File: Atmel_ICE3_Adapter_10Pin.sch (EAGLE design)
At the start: 2 parts

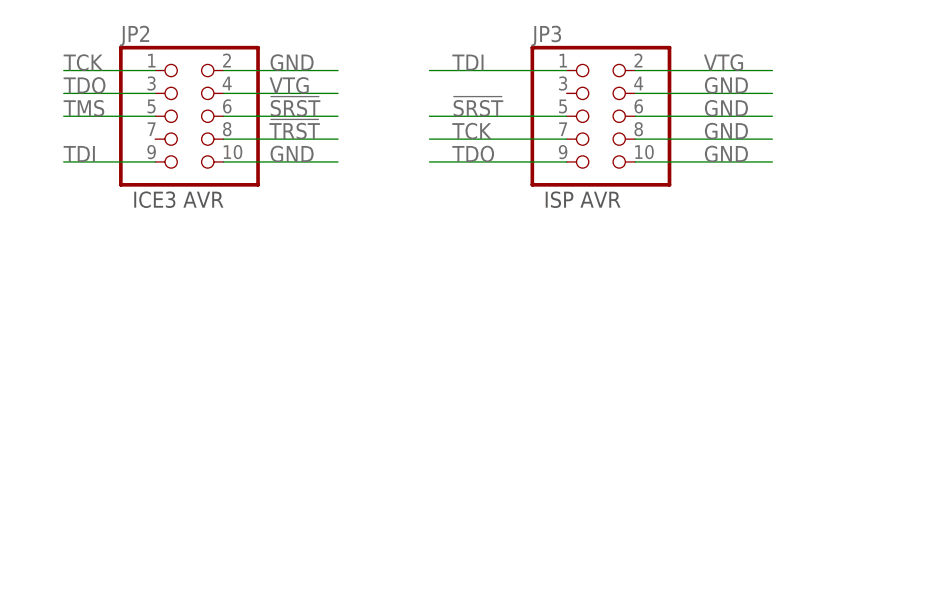
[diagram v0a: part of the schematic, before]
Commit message: Fix 6 pin wrong ICE3 header
Add 10 pin
Add gerber files
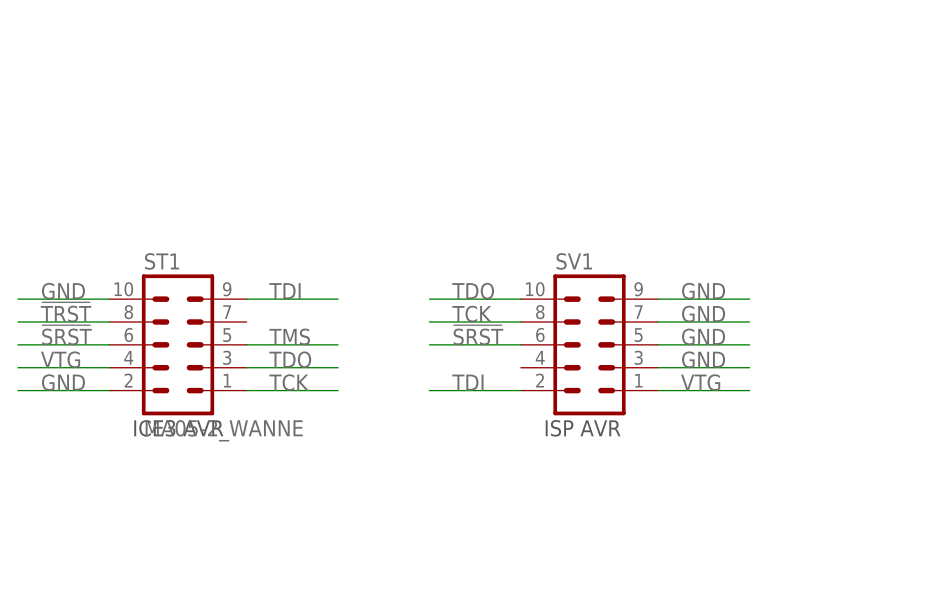
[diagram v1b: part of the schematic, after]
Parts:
- removed JP2: (no value), pinhead_2:PINHD-2X5_2.00
- removed JP3: (no value), pinhead_2:PINHD-2X5_2.54
- added ST1: MA05-2_WANNE, pin-header-1.27:MA05-2_WANNE
- added SV1: (no value), con-lstb:MA05-2
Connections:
- net !SRST: now also ST1.6, SV1.6; no longer JP2.6, JP3.5
- net !TRST: now also ST1.8; no longer JP2.8
- net GND: now also ST1.10, ST1.2, SV1.3, SV1.5, SV1.7, SV1.9; no longer JP2.10, JP2.2, JP3.10, JP3.4, JP3.6, JP3.8
- net TCK: now also ST1.1, SV1.8; no longer JP2.1, JP3.7
- net TDI: now also ST1.9, SV1.2; no longer JP2.9, JP3.1
- net TDO: now also ST1.3, SV1.10; no longer JP2.3, JP3.9
- net TMS: now also ST1.5; no longer JP2.5
- net VTG: now also ST1.4, SV1.1; no longer JP2.4, JP3.2
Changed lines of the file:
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@@
 </variantdefs>
 <classes>
-<class number="0" name="default" width="0.3" drill="0.3">
-<clearance class="0" value="0.3"/>
+<class number="0" name="default" width="0" drill="0">
 </class>
-<class number="1" name="pwr" width="0.5" drill="0.5">
-<clearance class="1" value="0.3"/>
+<class number="1" name="pwr" width="0" drill="0">
 </class>
 </classes>
 <parts>
-<part name="JP2" library="pinhead_2" deviceset="PINHD-2X5" device="_2.00"/>
-<part name="JP3" library="pinhead_2" deviceset="PINHD-2X5" device="_2.54"/>
 <part name="FRAME1" library="frames" deviceset="DINA4_L" device=""/>
+<part name="SV1" library="con-lstb" deviceset="MA05-2" device=""/>
+<part name="ST1" library="pin-header-1.27" deviceset="MA05-2_WANNE" device=""/>
 </parts>
 <sheets>
 <sheet>
 <plain>
-<text x="99.06" y="91.44" size="1.778" layer="97">ICE3 AVR</text>
-<text x="144.78" y="91.44" size="1.778" layer="97">ISP AVR</text>
+<text x="99.06" y="66.04" size="1.778" layer="97">ICE3 AVR</text>
+<text x="144.78" y="66.04" size="1.778" layer="97">ISP AVR</text>
 <text x="180.086" y="26.162" size="5.08" layer="97">Adapter ICE3 AVR</text>
 </plain>
 <instances>
-<instance part="JP2" gate="A" x="104.14" y="101.6"/>
-<instance part="JP3" gate="A" x="149.86" y="101.6"/>
 <instance part="FRAME1" gate="G$1" x="0" y="0"/>
 <instance part="FRAME1" gate="G$2" x="162.56" y="0"/>
+<instance part="SV1" gate="G$1" x="149.86" y="76.2"/>
+<instance part="ST1" gate="G$1" x="104.14" y="76.2"/>
 </instances>
 <busses>
@@
 <net name="TCK" class="0">
 <segment>
-<wire x1="101.6" y1="106.68" x2="91.44" y2="106.68" width="0.1524" layer="91"/>
-<label x="91.44" y="106.68" size="1.778" layer="95"/>
-<pinref part="JP2" gate="A" pin="1"/>
+<pinref part="SV1" gate="G$1" pin="8"/>
+<wire x1="142.24" y1="78.74" x2="132.08" y2="78.74" width="0.1524" layer="91"/>
+<label x="134.62" y="78.74" size="1.778" layer="95"/>
 </segment>
 <segment>
-<pinref part="JP3" gate="A" pin="7"/>
-<wire x1="147.32" y1="99.06" x2="132.08" y2="99.06" width="0.1524" layer="91"/>
-<label x="134.62" y="99.06" size="1.778" layer="95"/>
+<wire x1="111.76" y1="71.12" x2="121.92" y2="71.12" width="0.1524" layer="91"/>
+<label x="114.3" y="71.12" size="1.778" layer="95"/>
+<pinref part="ST1" gate="G$1" pin="1"/>
 </segment>
 </net>
 <net name="TDO" class="0">
 <segment>
-<wire x1="101.6" y1="104.14" x2="91.44" y2="104.14" width="0.1524" layer="91"/>
-<label x="91.44" y="104.14" size="1.778" layer="95"/>
-<pinref part="JP2" gate="A" pin="3"/>
+<pinref part="SV1" gate="G$1" pin="10"/>
+<wire x1="142.24" y1="81.28" x2="132.08" y2="81.28" width="0.1524" layer="91"/>
+<label x="134.62" y="81.28" size="1.778" layer="95"/>
 </segment>
 <segment>
-<pinref part="JP3" gate="A" pin="9"/>
-<wire x1="147.32" y1="96.52" x2="132.08" y2="96.52" width="0.1524" layer="91"/>
-<label x="134.62" y="96.52" size="1.778" layer="95"/>
+<wire x1="111.76" y1="73.66" x2="121.92" y2="73.66" width="0.1524" layer="91"/>
+<label x="114.3" y="73.66" size="1.778" layer="95"/>
+<pinref part="ST1" gate="G$1" pin="3"/>
 </segment>
 </net>
 <net name="TMS" class="0">
 <segment>
-<wire x1="101.6" y1="101.6" x2="91.44" y2="101.6" width="0.1524" layer="91"/>
-<label x="91.44" y="101.6" size="1.778" layer="95"/>
-<pinref part="JP2" gate="A" pin="5"/>
+<wire x1="111.76" y1="76.2" x2="121.92" y2="76.2" width="0.1524" layer="91"/>
+<label x="114.3" y="76.2" size="1.778" layer="95"/>
+<pinref part="ST1" gate="G$1" pin="5"/>
 </segment>
 </net>
 <net name="TDI" class="0">
 <segment>
-<wire x1="101.6" y1="96.52" x2="91.44" y2="96.52" width="0.1524" layer="91"/>
-<label x="91.44" y="96.52" size="1.778" layer="95"/>
-<pinref part="JP2" gate="A" pin="9"/>
+<pinref part="SV1" gate="G$1" pin="2"/>
+<wire x1="142.24" y1="71.12" x2="132.08" y2="71.12" width="0.1524" layer="91"/>
+<label x="134.62" y="71.12" size="1.778" layer="95"/>
 </segment>
 <segment>
-<pinref part="JP3" gate="A" pin="1"/>
-<wire x1="147.32" y1="106.68" x2="132.08" y2="106.68" width="0.1524" layer="91"/>
-<label x="134.62" y="106.68" size="1.778" layer="95"/>
+<wire x1="111.76" y1="81.28" x2="121.92" y2="81.28" width="0.1524" layer="91"/>
+<label x="114.3" y="81.28" size="1.778" layer="95"/>
+<pinref part="ST1" gate="G$1" pin="9"/>
 </segment>
 </net>
 <net name="GND" class="1">
 <segment>
-<wire x1="109.22" y1="96.52" x2="121.92" y2="96.52" width="0.1524" layer="91"/>
-<label x="114.3" y="96.52" size="1.778" layer="95"/>
-<pinref part="JP2" gate="A" pin="10"/>
+<pinref part="SV1" gate="G$1" pin="9"/>
+<wire x1="157.48" y1="81.28" x2="167.64" y2="81.28" width="0.1524" layer="91"/>
+<label x="160.02" y="81.28" size="1.778" layer="95"/>
 </segment>
 <segment>
-<wire x1="109.22" y1="106.68" x2="121.92" y2="106.68" width="0.1524" layer="91"/>
-<label x="114.3" y="106.68" size="1.778" layer="95"/>
-<pinref part="JP2" gate="A" pin="2"/>
+<pinref part="SV1" gate="G$1" pin="7"/>
+<wire x1="157.48" y1="78.74" x2="167.64" y2="78.74" width="0.1524" layer="91"/>
+<label x="160.02" y="78.74" size="1.778" layer="95"/>
 </segment>
 <segment>
-<pinref part="JP3" gate="A" pin="10"/>
-<wire x1="154.94" y1="96.52" x2="170.18" y2="96.52" width="0.1524" layer="91"/>
-<label x="162.56" y="96.52" size="1.778" layer="95"/>
+<pinref part="SV1" gate="G$1" pin="5"/>
+<wire x1="157.48" y1="76.2" x2="167.64" y2="76.2" width="0.1524" layer="91"/>
+<label x="160.02" y="76.2" size="1.778" layer="95"/>
 </segment>
 <segment>
-<pinref part="JP3" gate="A" pin="8"/>
-<wire x1="154.94" y1="99.06" x2="170.18" y2="99.06" width="0.1524" layer="91"/>
-<label x="162.56" y="99.06" size="1.778" layer="95"/>
+<pinref part="SV1" gate="G$1" pin="3"/>
+<wire x1="157.48" y1="73.66" x2="167.64" y2="73.66" width="0.1524" layer="91"/>
+<label x="160.02" y="73.66" size="1.778" layer="95"/>
 </segment>
 <segment>
-<pinref part="JP3" gate="A" pin="6"/>
-<wire x1="154.94" y1="101.6" x2="170.18" y2="101.6" width="0.1524" layer="91"/>
-<label x="162.56" y="101.6" size="1.778" layer="95"/>
+<wire x1="96.52" y1="81.28" x2="86.36" y2="81.28" width="0.1524" layer="91"/>
+<label x="88.9" y="81.28" size="1.778" layer="95"/>
+<pinref part="ST1" gate="G$1" pin="10"/>
 </segment>
 <segment>
-<pinref part="JP3" gate="A" pin="4"/>
-<wire x1="154.94" y1="104.14" x2="170.18" y2="104.14" width="0.1524" layer="91"/>
-<label x="162.56" y="104.14" size="1.778" layer="95"/>
+<wire x1="96.52" y1="71.12" x2="86.36" y2="71.12" width="0.1524" layer="91"/>
+<label x="88.9" y="71.12" size="1.778" layer="95"/>
+<pinref part="ST1" gate="G$1" pin="2"/>
 </segment>
 </net>
 <net name="!TRST" class="0">
 <segment>
-<wire x1="109.22" y1="99.06" x2="121.92" y2="99.06" width="0.1524" layer="91"/>
-<label x="114.3" y="99.06" size="1.778" layer="95"/>
-<pinref part="JP2" gate="A" pin="8"/>
+<wire x1="96.52" y1="78.74" x2="86.36" y2="78.74" width="0.1524" layer="91"/>
+<label x="88.9" y="78.74" size="1.778" layer="95"/>
+<pinref part="ST1" gate="G$1" pin="8"/>
 </segment>
 </net>
 <net name="VTG" class="1">
 <segment>
-<wire x1="109.22" y1="104.14" x2="121.92" y2="104.14" width="0.1524" layer="91"/>
-<label x="114.3" y="104.14" size="1.778" layer="95"/>
-<pinref part="JP2" gate="A" pin="4"/>
+<wire x1="96.52" y1="73.66" x2="86.36" y2="73.66" width="0.1524" layer="91"/>
+<label x="88.9" y="73.66" size="1.778" layer="95"/>
+<pinref part="ST1" gate="G$1" pin="4"/>
 </segment>
 <segment>
-<pinref part="JP3" gate="A" pin="2"/>
-<wire x1="154.94" y1="106.68" x2="170.18" y2="106.68" width="0.1524" layer="91"/>
-<label x="162.56" y="106.68" size="1.778" layer="95"/>
+<pinref part="SV1" gate="G$1" pin="1"/>
+<wire x1="157.48" y1="71.12" x2="167.64" y2="71.12" width="0.1524" layer="91"/>
+<label x="160.02" y="71.12" size="1.778" layer="95"/>
 </segment>
 </net>
 <net name="!SRST" class="0">
 <segment>
-<wire x1="109.22" y1="101.6" x2="121.92" y2="101.6" width="0.1524" layer="91"/>
-<label x="114.3" y="101.6" size="1.778" layer="95"/>
-<pinref part="JP2" gate="A" pin="6"/>
+<pinref part="SV1" gate="G$1" pin="6"/>
+<wire x1="142.24" y1="76.2" x2="132.08" y2="76.2" width="0.1524" layer="91"/>
+<label x="134.62" y="76.2" size="1.778" layer="95"/>
 </segment>
 <segment>
-<pinref part="JP3" gate="A" pin="5"/>
-<wire x1="147.32" y1="101.6" x2="132.08" y2="101.6" width="0.1524" layer="91"/>
-<label x="134.62" y="101.6" size="1.778" layer="95"/>
+<wire x1="96.52" y1="76.2" x2="86.36" y2="76.2" width="0.1524" layer="91"/>
+<label x="88.9" y="76.2" size="1.778" layer="95"/>
+<pinref part="ST1" gate="G$1" pin="6"/>
 </segment>
 </net>
